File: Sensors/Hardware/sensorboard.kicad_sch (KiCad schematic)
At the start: 62 parts, among them J1 RBUS, U1 ESP32-S3, Y1 40MHz±10ppm

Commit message: changed SPI layout
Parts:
- removed TP_VSPI_MISO1, TP_VSPI_MOSI1, TP_VSPI_SCLK1: TestPoint, TestPoint:TestPoint_Pad_D1.0mm, symbol Connector:TestPoint
- R20: footprint (none) -> Resistor_SMD:R_0402_1005Metric
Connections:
- net VSPI_MOSI is gone; now on net SD1_DET: U1.10 (GPIO5/ADC1_CH4)
- net SD1_DET: no longer U1.51 (GPIO45)
- net VSPI_MISO: no longer names the net of U1.7 (GPIO2/ADC1_CH1)
- net VSPI_SCLK: no longer names the net of U1.9 (GPIO4/ADC1_CH3)
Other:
- moved on the sheet: TP_SD1_DET1

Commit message: fixed the CAN
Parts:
- C13, C14: footprint Capacitor_SMD:C_0603_1608Metric -> Capacitor_SMD:C_0402_1005Metric
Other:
- sheet CAN-BUS ports: added CAN_HIGH, CAN_LOW; removed none
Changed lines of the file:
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@@
+    (stroke (width 0) (type default))
+  )
+  (wire (pts (xy 228.6 68.58) (xy 236.22 68.58))
     (stroke (width 0) (type default))
   )
@@
   )
   (wire (pts (xy 146.05 148.59) (xy 158.75 148.59))
+    (stroke (width 0) (type default))
+  )
+  (wire (pts (xy 228.6 66.04) (xy 236.22 66.04))
     (stroke (width 0) (type default))
   )
@@
     (effects (font (size 1.27 1.27)) (justify right bottom))
   )
+  (label "CAN-" (at 236.22 68.58 0) (fields_autoplaced)
+    (effects (font (size 1.27 1.27)) (justify left bottom))
+  )
   (label "MOSI" (at 147.32 137.16 180) (fields_autoplaced)
     (effects (font (size 1.27 1.27)) (justify right bottom))
@@
   )
   (label "BOOT" (at 62.23 132.08 0) (fields_autoplaced)
+    (effects (font (size 1.27 1.27)) (justify left bottom))
+  )
+  (label "CAN+" (at 236.22 66.04 0) (fields_autoplaced)
     (effects (font (size 1.27 1.27)) (justify left bottom))
   )
@@
       (effects (font (size 1.27 1.27)) (justify left))
     )
-    (property "Footprint" "Capacitor_SMD:C_0603_1608Metric" (at 165.1 148.59 0)
+    (property "Footprint" "Capacitor_SMD:C_0402_1005Metric" (at 165.1 148.59 0)
       (effects (font (size 1.27 1.27)) hide)
     )
@@
       (effects (font (size 1.27 1.27)) (justify left))
     )
-    (property "Footprint" "Capacitor_SMD:C_0603_1608Metric" (at 166.37 160.02 0)
+    (property "Footprint" "Capacitor_SMD:C_0402_1005Metric" (at 166.37 160.02 0)
       (effects (font (size 1.27 1.27)) hide)
     )
@@
       (effects (font (size 1.27 1.27)) (justify right))
     )
+    (pin "CAN_HIGH" bidirectional (at 228.6 66.04 0)
+      (effects (font (size 1.27 1.27)) (justify right))
+    )
+    (pin "CAN_LOW" bidirectional (at 228.6 68.58 0)
+      (effects (font (size 1.27 1.27)) (justify right))
+    )

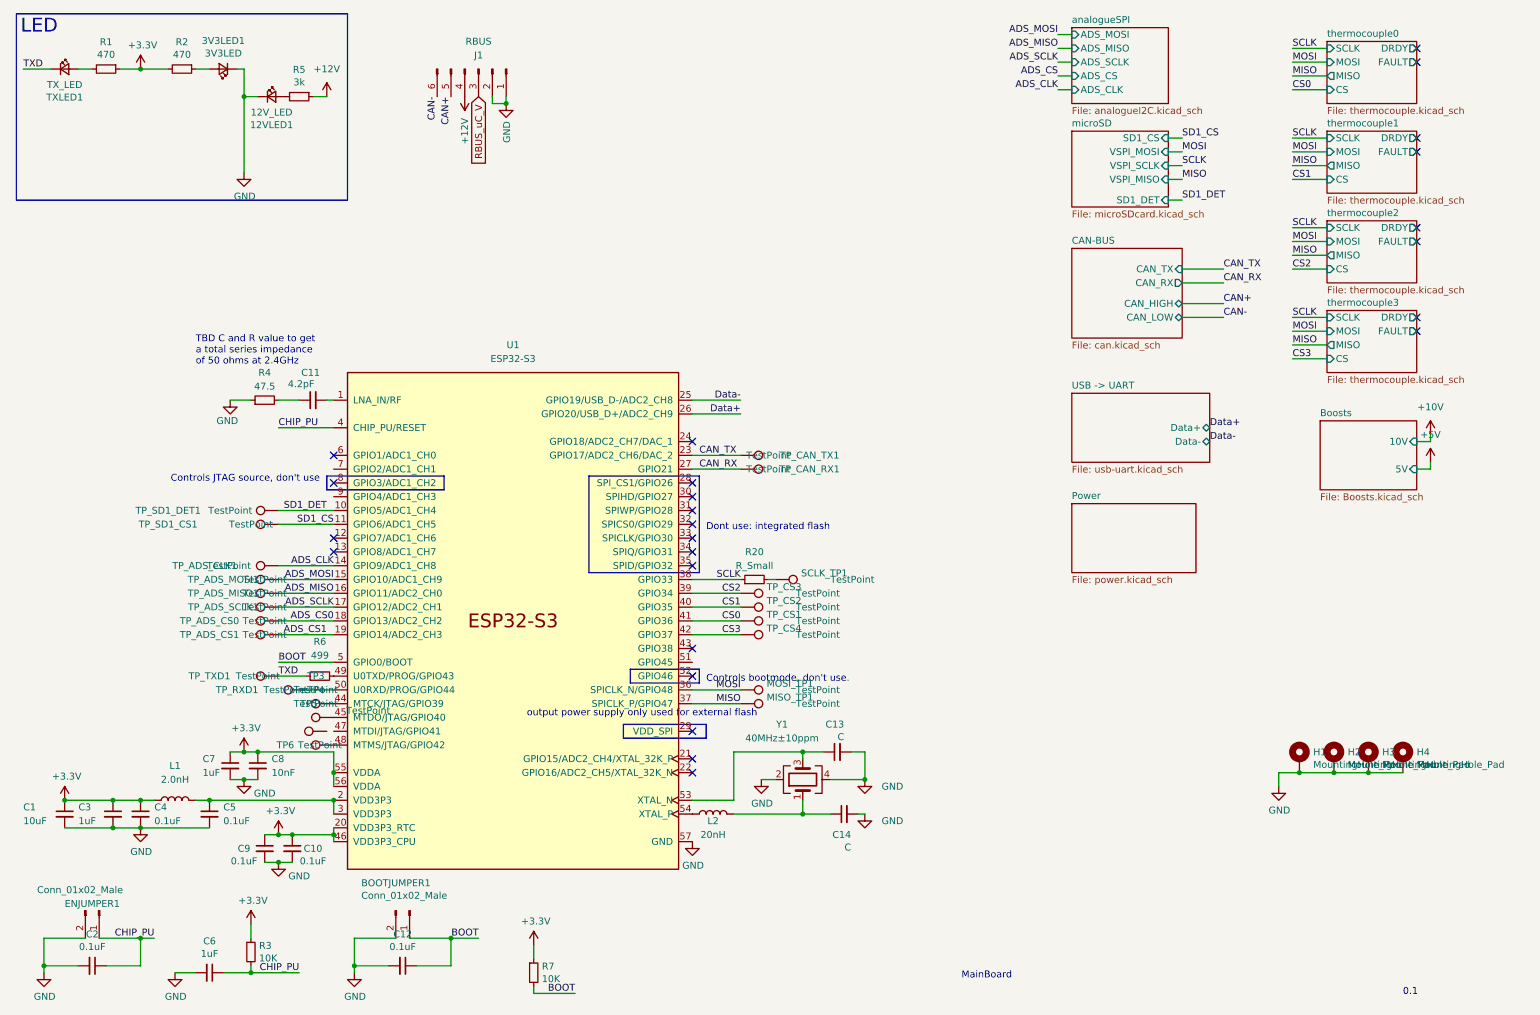
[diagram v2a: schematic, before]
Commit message: ADS line fix and schematic
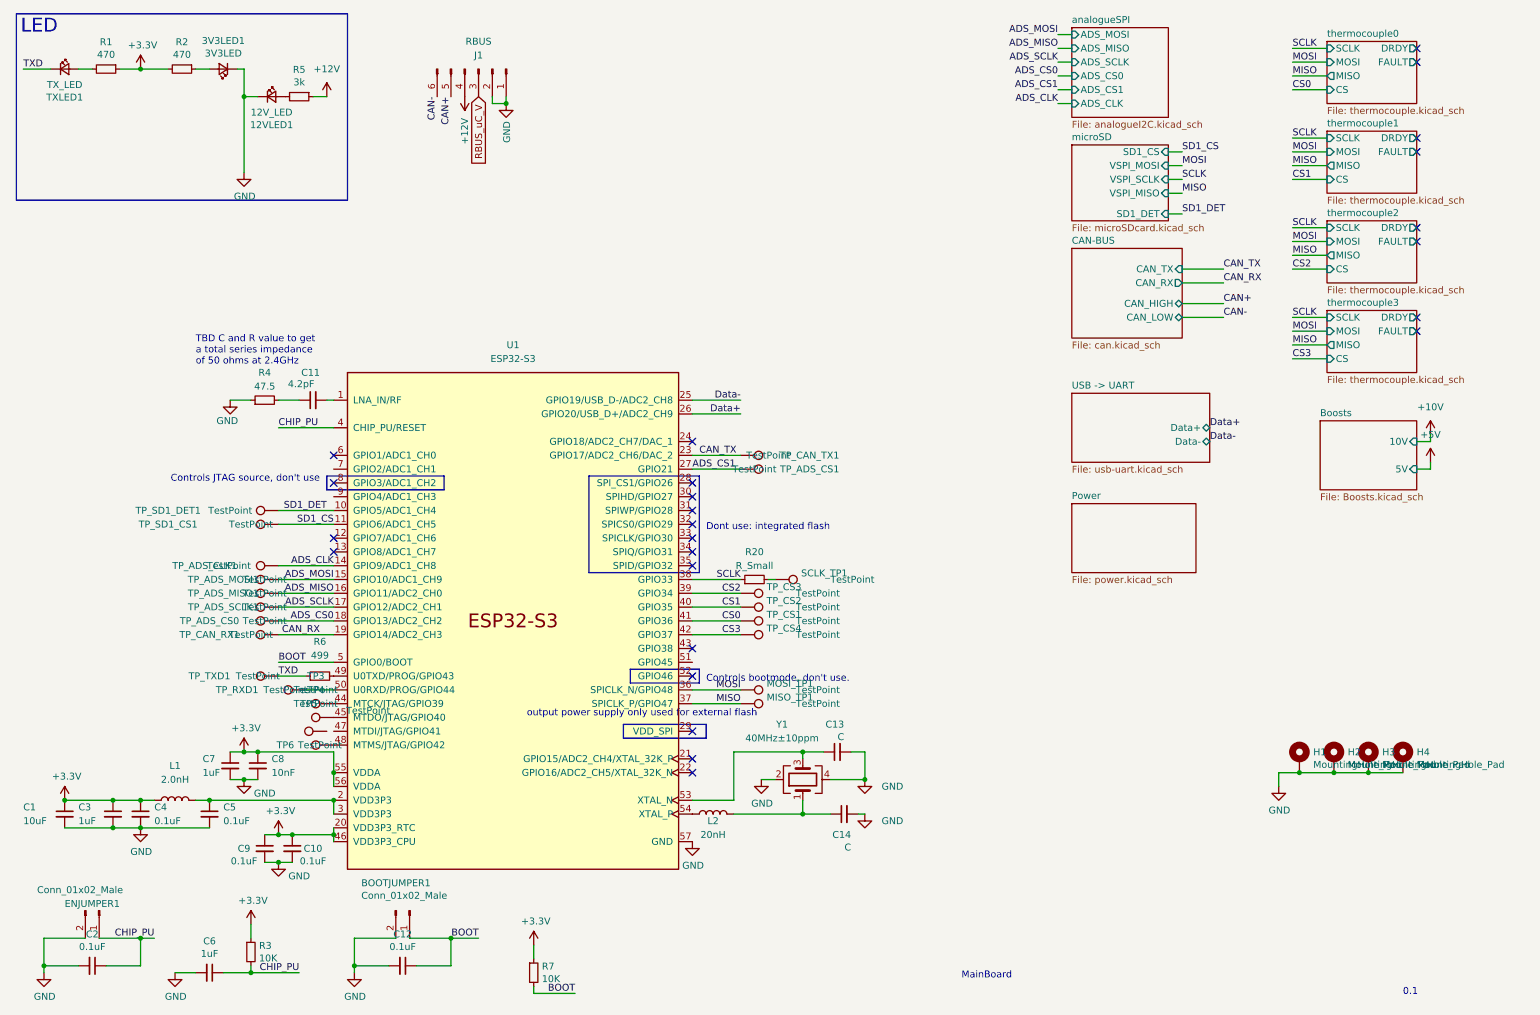
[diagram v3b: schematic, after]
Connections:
- net ADS_CS1: now also U1.27 (GPIO21); no longer U1.19 (GPIO14/ADC2_CH3)
- net CAN_RX: now also U1.19 (GPIO14/ADC2_CH3); no longer U1.27 (GPIO21)
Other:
- sheet analogueSPI ports: added ADS_CS0, ADS_CS1; removed ADS_CS
- moved on the sheet: TP_ADS_CS1, TP_CAN_RX1

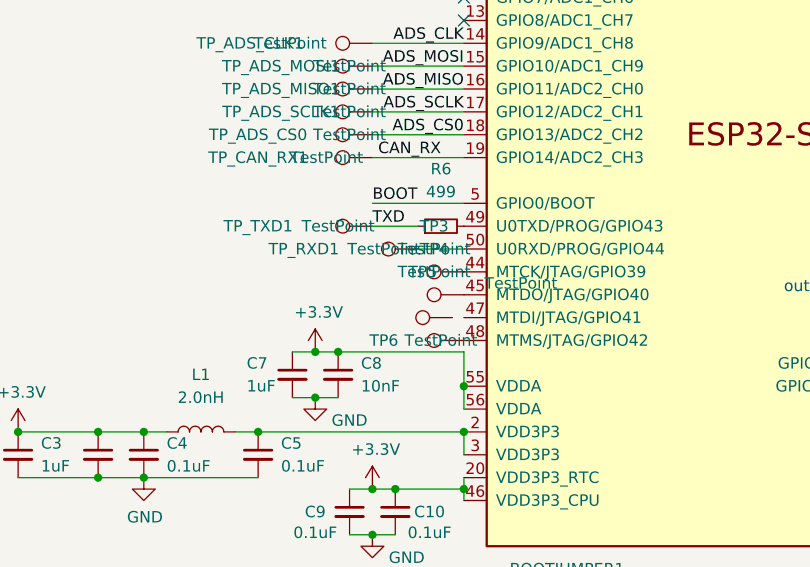
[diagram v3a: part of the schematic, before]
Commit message: optimised the boost layouts
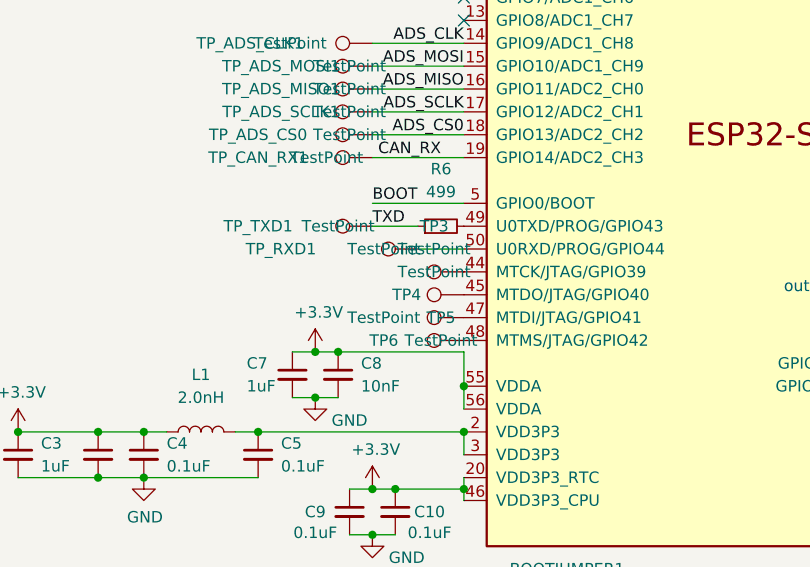
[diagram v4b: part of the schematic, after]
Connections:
- net at U1.47 (MTDI/JTAG/GPIO41): now also TP5.1
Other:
- moved on the sheet: TP5
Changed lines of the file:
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@@
   )
   (symbol (lib_id "Connector:TestPoint") (at 72.39 142.24 90) (unit 1)
-    (in_bom yes) (on_board yes) (dnp no) (fields_autoplaced)
-    (property "Reference" "TP4" (at 69.088 137.16 90)
+    (in_bom yes) (on_board yes) (dnp no)
+    (property "Reference" "TP4" (at 66.04 142.24 90)
       (effects (font (size 1.27 1.27)))
     )
@@
   (symbol (lib_id "Connector:TestPoint") (at 67.31 137.16 90) (unit 1)
     (in_bom yes) (on_board yes) (dnp no)
-    (property "Reference" "TP_RXD1" (at 54.61 137.16 90)
+    (property "Reference" "TP_RXD1" (at 52.07 137.16 90)
       (effects (font (size 1.27 1.27)))
     )
@@
     )
   )
-  (symbol (lib_id "Connector:TestPoint") (at 71.12 144.78 90) (unit 1)
-    (in_bom yes) (on_board yes) (dnp no)
-    (property "Reference" "TP5" (at 67.818 139.7 90)
-      (effects (font (size 1.27 1.27)))
-    )
-    (property "Value" "TestPoint" (at 78.74 140.97 90)
-      (effects (font (size 1.27 1.27)))
-    )
-    (property "Footprint" "TestPoint:TestPoint_Pad_D1.0mm" (at 71.12 139.7 0)
-      (effects (font (size 1.27 1.27)) hide)
-    )
-    (property "Datasheet" "~" (at 71.12 139.7 0)
-      (effects (font (size 1.27 1.27)) hide)
-    )
+  (symbol (lib_id "Connector:TestPoint") (at 72.39 144.78 90) (unit 1)
+    (in_bom yes) (on_board yes) (dnp no)
+    (property "Reference" "TP5" (at 69.85 144.78 90)
+      (effects (font (size 1.27 1.27)))
+    )
+    (property "Value" "TestPoint" (at 63.5 144.78 90)
+      (effects (font (size 1.27 1.27)))
+    )
+    (property "Footprint" "TestPoint:TestPoint_Pad_D1.0mm" (at 72.39 139.7 0)
+      (effects (font (size 1.27 1.27)) hide)
+    )
+    (property "Datasheet" "~" (at 72.39 139.7 0)
+      (effects (font (size 1.27 1.27)) hide)
+    )

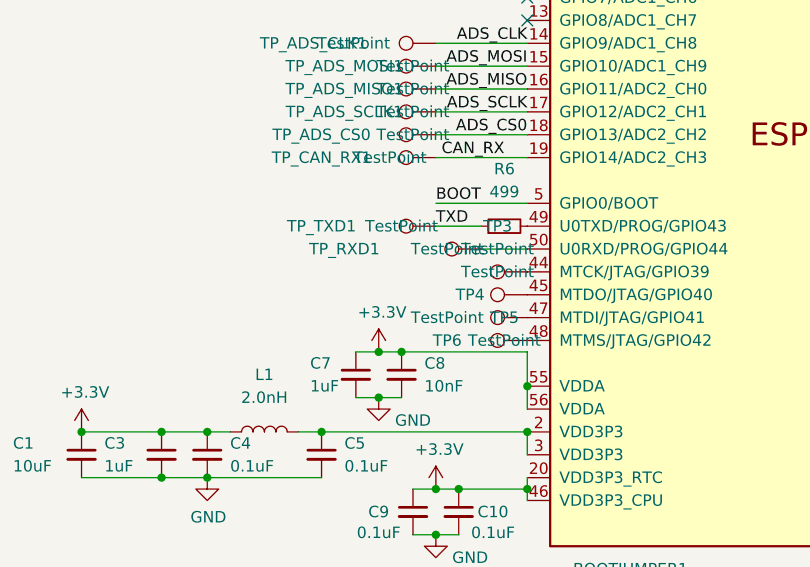
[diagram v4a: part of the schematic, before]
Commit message: JTAG tps fixed and teardrops
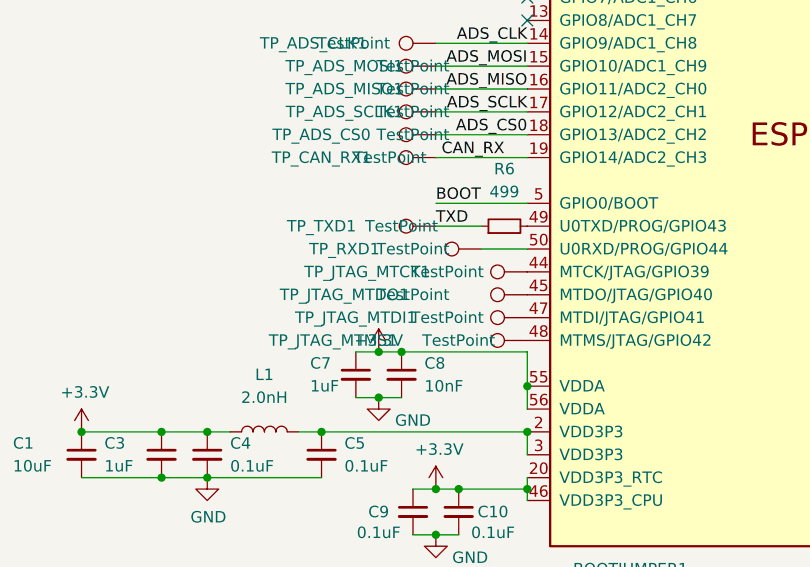
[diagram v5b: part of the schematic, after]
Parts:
- renumbered TP3 to TP_JTAG_MTCK1, TP5 to TP_JTAG_MTDI1, TP4 to TP_JTAG_MTDO1, TP6 to TP_JTAG_MTMS1
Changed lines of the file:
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@@
   (symbol (lib_id "Connector:TestPoint") (at 72.39 147.32 90) (unit 1)
     (in_bom yes) (on_board yes) (dnp no)
-    (property "Reference" "TP6" (at 63.5 147.32 90)
-      (effects (font (size 1.27 1.27)))
-    )
-    (property "Value" "TestPoint" (at 69.85 147.32 90)
+    (property "Reference" "TP_JTAG_MTMS1" (at 50.8 147.32 90)
+      (effects (font (size 1.27 1.27)))
+    )
+    (property "Value" "TestPoint" (at 64.77 147.32 90)
       (effects (font (size 1.27 1.27)))
     )
@@
       (project "sensorboard"
         (path "/26801cfb-b53b-4a6a-a2f4-5f4986565765"
-          (reference "TP6") (unit 1)
+          (reference "TP_JTAG_MTMS1") (unit 1)
         )
       )
@@
       (effects (font (size 1.27 1.27)) hide)
     )
-    (property "Value" "+3.3V" (at 56.261 144.1958 0)
+    (property "Value" "+3.3V" (at 55.88 147.32 0)
       (effects (font (size 1.27 1.27)))
     )
@@
   (symbol (lib_id "Connector:TestPoint") (at 72.39 142.24 90) (unit 1)
     (in_bom yes) (on_board yes) (dnp no)
-    (property "Reference" "TP4" (at 66.04 142.24 90)
-      (effects (font (size 1.27 1.27)))
-    )
-    (property "Value" "TestPoint" (at 69.088 139.7 90)
+    (property "Reference" "TP_JTAG_MTDO1" (at 52.07 142.24 90)
+      (effects (font (size 1.27 1.27)))
+    )
+    (property "Value" "TestPoint" (at 59.69 142.24 90)
       (effects (font (size 1.27 1.27)))
     )
@@
       (project "sensorboard"
         (path "/26801cfb-b53b-4a6a-a2f4-5f4986565765"
-          (reference "TP4") (unit 1)
+          (reference "TP_JTAG_MTDO1") (unit 1)
         )
       )
@@
       (effects (font (size 1.27 1.27)))
     )
-    (property "Value" "TestPoint" (at 63.5 137.16 90)
+    (property "Value" "TestPoint" (at 59.69 137.16 90)
       (effects (font (size 1.27 1.27)))
     )
@@
   (symbol (lib_id "Connector:TestPoint") (at 72.39 144.78 90) (unit 1)
     (in_bom yes) (on_board yes) (dnp no)
-    (property "Reference" "TP5" (at 69.85 144.78 90)
+    (property "Reference" "TP_JTAG_MTDI1" (at 53.34 144.78 90)
       (effects (font (size 1.27 1.27)))
     )
@@
       (project "sensorboard"
         (path "/26801cfb-b53b-4a6a-a2f4-5f4986565765"
-          (reference "TP5") (unit 1)
+          (reference "TP_JTAG_MTDI1") (unit 1)
         )
       )
@@
   )
   (symbol (lib_id "Connector:TestPoint") (at 72.39 139.7 90) (unit 1)
-    (in_bom yes) (on_board yes) (dnp no) (fields_autoplaced)
-    (property "Reference" "TP3" (at 69.088 134.62 90)
-      (effects (font (size 1.27 1.27)))
-    )
-    (property "Value" "TestPoint" (at 69.088 137.16 90)
+    (in_bom yes) (on_board yes) (dnp no)
+    (property "Reference" "TP_JTAG_MTCK1" (at 54.61 139.7 90)
+      (effects (font (size 1.27 1.27)))
+    )
+    (property "Value" "TestPoint" (at 63.5 139.7 90)
       (effects (font (size 1.27 1.27)))
     )
@@
       (project "sensorboard"
         (path "/26801cfb-b53b-4a6a-a2f4-5f4986565765"
-          (reference "TP3") (unit 1)
-        )
-      )
+          (reference "TP_JTAG_MTCK1") (unit 1)
+        )
+      )

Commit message: termination resistor and DRC cleanup
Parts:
- R20: value R_Small -> 68.1R
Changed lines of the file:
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@@
   (symbol (lib_id "Connector:TestPoint") (at 67.31 137.16 90) (unit 1)
     (in_bom yes) (on_board yes) (dnp no)
-    (property "Reference" "TP_RXD1" (at 52.07 137.16 90)
+    (property "Reference" "TP_RXD1" (at 48.26 137.16 90)
       (effects (font (size 1.27 1.27)))
     )
@@
       (effects (font (size 1.27 1.27)))
     )
-    (property "Value" "R_Small" (at 149.86 114.3 90)
+    (property "Value" "68.1R" (at 149.86 114.3 90)
       (effects (font (size 1.27 1.27)))
     )

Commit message: update
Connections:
- net ADS_MISO renamed SD_MISO
- net ADS_MOSI renamed SD_MOSI
- net ADS_SCLK renamed SD_SCLK
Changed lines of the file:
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@@
     (effects (font (size 1.27 1.27)) (justify right bottom))
   )
-  (label "ADS_MOSI" (at 72.39 116.84 180) (fields_autoplaced)
+  (label "SD_MOSI" (at 72.39 116.84 180) (fields_autoplaced)
     (effects (font (size 1.27 1.27)) (justify right bottom))
   )
@@
     (effects (font (size 1.27 1.27)) (justify left bottom))
   )
-  (label "MISO" (at 228.6 45.72 0) (fields_autoplaced)
+  (label "SD_MISO" (at 228.6 45.72 0) (fields_autoplaced)
     (effects (font (size 1.27 1.27)) (justify left bottom))
   )
@@
     (effects (font (size 1.27 1.27)) (justify right bottom))
   )
-  (label "ADS_SCLK" (at 205.74 21.59 180) (fields_autoplaced)
-    (effects (font (size 1.27 1.27)) (justify right bottom))
-  )
-  (label "ADS_MISO" (at 72.39 119.38 180) (fields_autoplaced)
-    (effects (font (size 1.27 1.27)) (justify right bottom))
-  )
-  (label "ADS_MOSI" (at 205.74 16.51 180) (fields_autoplaced)
+  (label "SCLK" (at 205.74 21.59 180) (fields_autoplaced)
+    (effects (font (size 1.27 1.27)) (justify right bottom))
+  )
+  (label "SD_MISO" (at 72.39 119.38 180) (fields_autoplaced)
+    (effects (font (size 1.27 1.27)) (justify right bottom))
+  )
+  (label "MOSI" (at 205.74 16.51 180) (fields_autoplaced)
     (effects (font (size 1.27 1.27)) (justify right bottom))
   )
@@
     (effects (font (size 1.27 1.27)) (justify right bottom))
   )
-  (label "SCLK" (at 228.6 43.18 0) (fields_autoplaced)
+  (label "SD_SCLK" (at 228.6 43.18 0) (fields_autoplaced)
     (effects (font (size 1.27 1.27)) (justify left bottom))
   )
@@
     (effects (font (size 1.27 1.27)) (justify right bottom))
   )
-  (label "MOSI" (at 228.6 40.64 0) (fields_autoplaced)
+  (label "SD_MOSI" (at 228.6 40.64 0) (fields_autoplaced)
     (effects (font (size 1.27 1.27)) (justify left bottom))
   )
@@
     (effects (font (size 1.27 1.27)) (justify right bottom))
   )
-  (label "ADS_SCLK" (at 72.39 121.92 180) (fields_autoplaced)
+  (label "SD_SCLK" (at 72.39 121.92 180) (fields_autoplaced)
     (effects (font (size 1.27 1.27)) (justify right bottom))
   )
@@
     (effects (font (size 1.27 1.27)) (justify left bottom))
   )
-  (label "ADS_MISO" (at 205.74 19.05 180) (fields_autoplaced)
+  (label "MISO" (at 205.74 19.05 180) (fields_autoplaced)
     (effects (font (size 1.27 1.27)) (justify right bottom))
   )
@@
       (effects (font (size 1.27 1.27)))
     )
-    (property "Value" "TestPoint" (at 59.69 116.84 90)
-      (effects (font (size 1.27 1.27)))
-    )
+    (property "Value" "TestPoint" (at 58.42 111.76 90)
+      (effects (font (size 1.27 1.27)))
+    )

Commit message: switched tc references
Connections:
- net CS0: now also U1.42 (GPIO37); no longer U1.41 (GPIO36)
- net CS1: now also U1.41 (GPIO36); no longer U1.40 (GPIO35)
- net CS2: now also U1.40 (GPIO35); no longer U1.39 (GPIO34)
- net CS3: now also U1.39 (GPIO34); no longer U1.42 (GPIO37)
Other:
- moved on the sheet: TP_CS1, TP_CS2, TP_CS3, TP_CS4
